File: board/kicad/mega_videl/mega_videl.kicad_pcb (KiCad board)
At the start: 10 copper layers, 70 x 89 mm, 218 parts, among them J1 Conn_02x07_Odd_Even, J2 Conn_01x04, J4 FPGA JTAG, J5 Conn_02x25_Odd_Even, J6 Conn_02x25_Odd_Even, U1 TPS51200DRCR, U10 TXV0108RGYR, U11 USB3300-EZK, U12 AP2553AW6-7, U13 PI6CG33201CZDIEX, U14 LAN9220-ABZJ, U15 PCA9546APWR, U16 HC-USB3.0-L168-WP, U17 CDCBT1001DPWR, U18 M25PX32-VMW, U19 TMDS1204IRNQR, U2 MT41K256M16LY, U20 TPD4E02B04DQA, U21 TPD4E02B04DQA, U22 TPD4E02B04DQA, U3 MT41K256M16LY, U4 TPS62903RPJR, U5 TPS7A2025PDBVR, U6 74LVC245ABQ, U7 TPS62903RPJR, U8 XLH335074.250000X, U9 5CFGXFC4F23, Y1 24MHz, Y2 25MHz, Y3 25MHz, Y4 ASE-50MHz

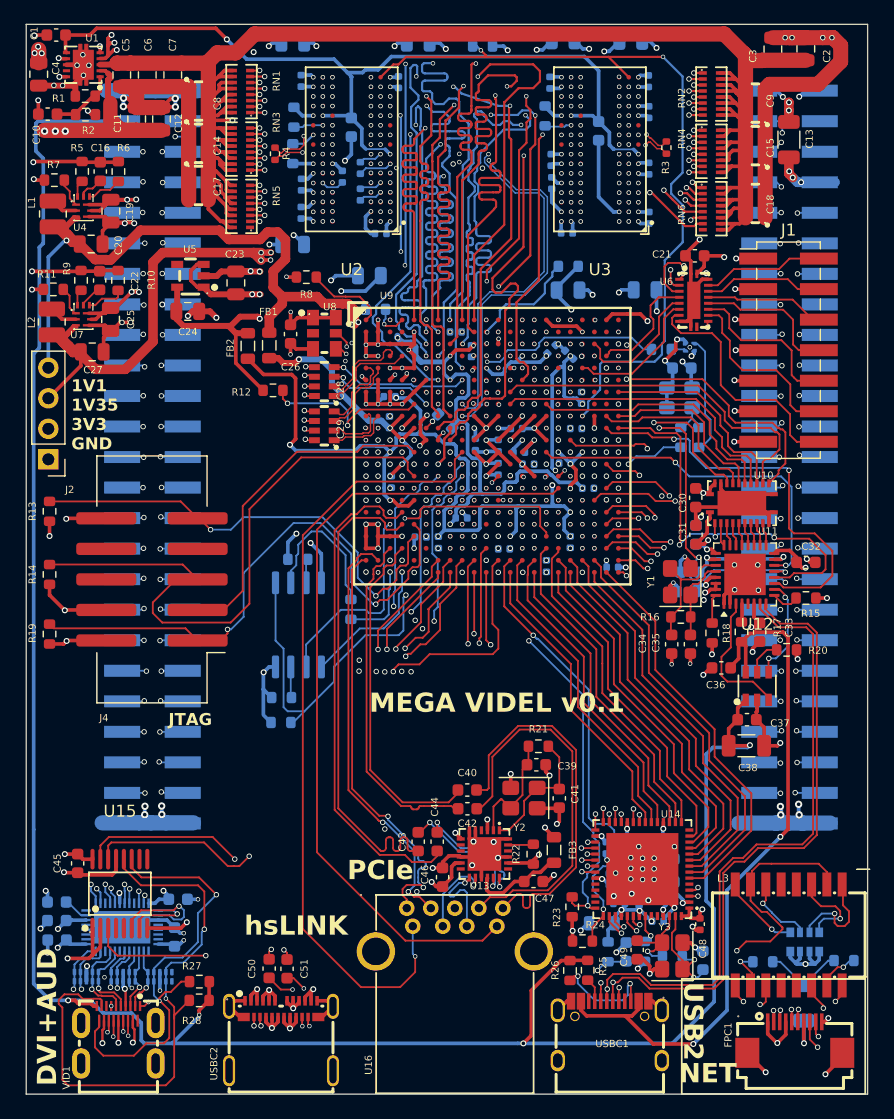
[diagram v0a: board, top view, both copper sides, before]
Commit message: Made board narrower so it fits next to CT60 SDRAM. Moved JTAG over slightly - more height
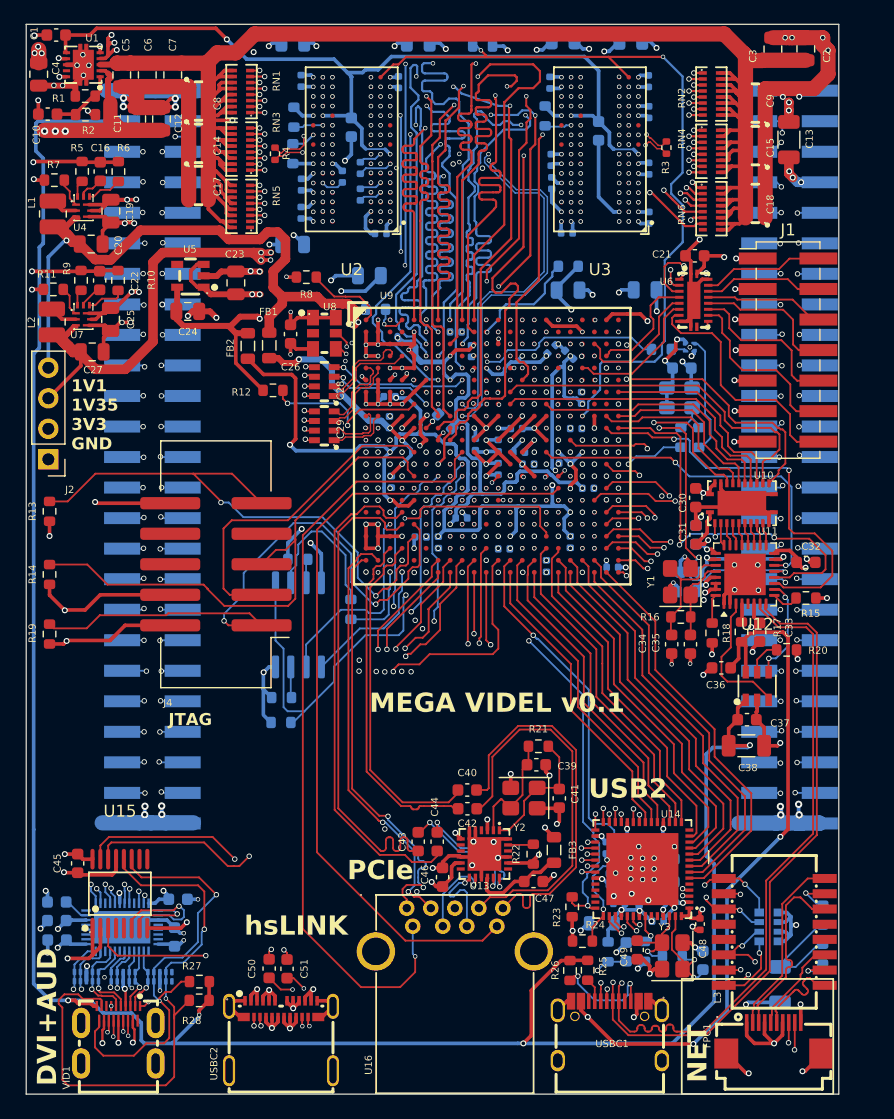
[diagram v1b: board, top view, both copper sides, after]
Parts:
- moved J4 5.47 mm to (45.3, 68.9)
- moved R47 5.02 mm to (95.8, 101.4), turned to 90 degrees
- moved R46 4.17 mm to (95.8, 98.1), turned to -90 degrees
- moved RN7 3.24 mm to (91.3, 99.1), turned to 90 degrees
- moved C122 2.49 mm to (92.2, 103.9)
- moved FPC1 1.75 mm to (91.7, 108.3)
- moved L3 1.24 mm to (91.7, 99.5), turned to -90 degrees
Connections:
- RN7 pad 3: /Ethernet/TPI_P -> /Ethernet/TPI_N
- RN7 pad 4: /Ethernet/TPI_N -> /Ethernet/TPI_P
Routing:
- net /Ethernet/TPI_N: track 26.1 -> 14.5 mm, vias 2 -> 3
- net /Ethernet/TPI_P: track 26.5 -> 15.9 mm, vias 2 -> 3
- net GND: track 474.0 -> 484.1 mm
- net /Ethernet/TPO_P: track 30.4 -> 20.9 mm, vias 2 -> 3
- net Net-(L3-RCT): track 36.1 -> 27.4 mm, vias 2 -> 3
- net /fpga/TDI: track 40.4 -> 49.1 mm
- net /Ethernet/RJTX_P: track 8.33 -> 15.3 mm, vias 2 -> 0
- net /Ethernet/RJTX_N: track 8.42 -> 15.3 mm, vias 2 -> 0
- net /fpga/TCK: track 47.2 -> 52.5 mm
- net +3V3: track 138.9 -> 144.0 mm
- net /Ethernet/TPO_N: track 27.9 -> 23.0 mm, vias 2 -> 3
- net /Ethernet/LED2: track 30.9 -> 26.6 mm
- net /fpga/TMS: track 51.5 -> 47.3 mm
- net /usb2/USBVBUSE: track 60.0 -> 63.3 mm, vias 2 -> 4
- net /usb2/USBD_P: track 54.4 -> 57.6 mm
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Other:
- board size 70 x 89 mm -> 67.6 x 89 mm
